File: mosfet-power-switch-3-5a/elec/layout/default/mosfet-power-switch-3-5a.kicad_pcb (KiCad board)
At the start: 2 copper layers, 225.7 x 100.8 mm, 0 parts

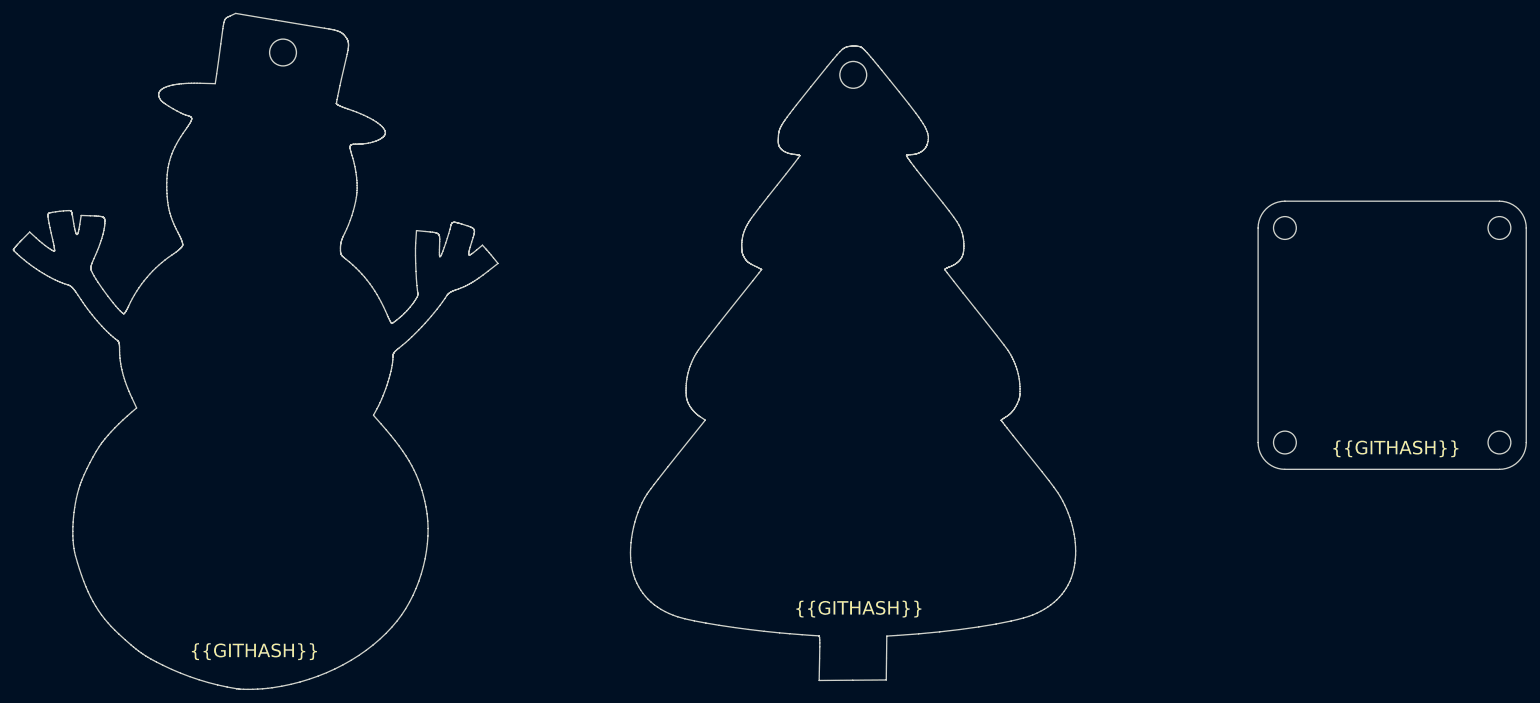
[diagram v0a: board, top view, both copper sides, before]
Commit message: placed components on board
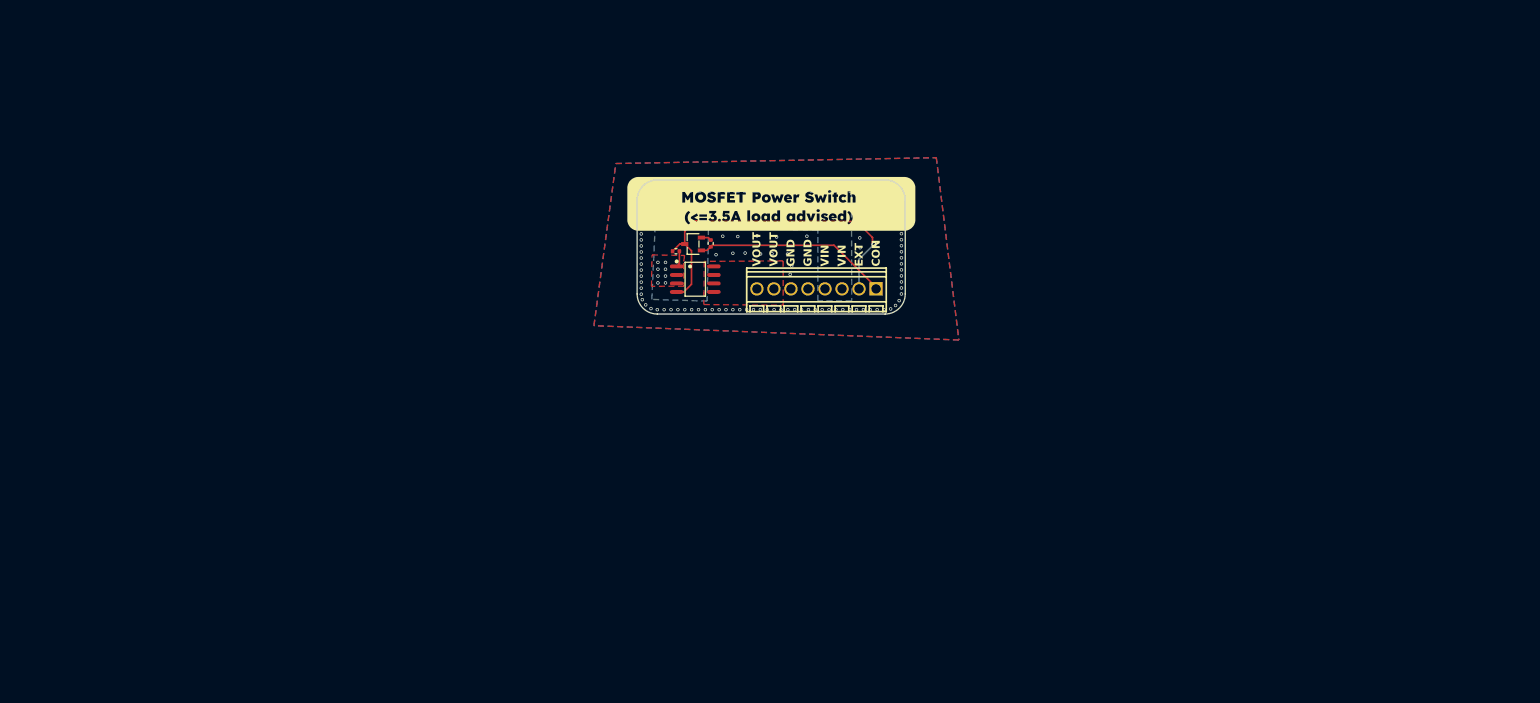
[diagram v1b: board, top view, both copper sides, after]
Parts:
- added Q1: , lib:SOIC-8_L4.9-W3.9-P1.27-LS6.0-BL, F.Cu at (137.7, 89.4)
- added Q2: , lib:SOT-23-3_L2.9-W1.6-P1.90-LS2.8-BR, F.Cu at (137.3, 84.2)
- added R1: 62.5mW Thick Film Resistors 50V ±100ppm/℃ ±1% 100kΩ 0402 Ch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, lib:R0402, F.Cu at (134.8, 85.3)
- added R2: 62.5mW Thick Film Resistors 50V ±100ppm/℃ ±1% 100kΩ 0402 Ch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, lib:R0402, F.Cu at (140.0, 84.1)
- added U1: , lib:CONN-TH_XY308-2.54-8P, F.Cu at (155.7, 90.9)
- added U2: , lib:MountingHole_3.2mm_M3, F.Cu at (133.2, 78.8)
- added U3: , lib:MountingHole_3.2mm_M3, F.Cu at (164.7, 78.9)
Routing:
- net _2: track 0.00 -> 51.8 mm, vias 0 -> 1
- net control: track 0.00 -> 29.3 mm
- net mosfet_power_switch-vcc: track 0.00 -> 2.43 mm, vias 0 -> 8
- net gnd: track 0.00 -> 1.53 mm, vias 0 -> 159
- added copper zone on B.Cu, net gnd
- added copper zone on F.Cu, net gnd
- added copper zone on B.Cu, net mosfet_power_switch-vcc
- added copper zone on F.Cu, net mosfet_power_switch-vcc
- added copper zone on F.Cu, net mosfet_power_switch-vcc-1
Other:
- board size 225.7 x 100.8 mm -> 40 x 20 mm
- board text added: "CON"
- board text added: "EXT"
- board text added: "GND"
- board text added: "Source files:"
- board text added: "VIN"
- board text added: "VOUT"
- board text added: "bit.ly/4b9zOe4"
- board text added: "designed by glowingkitty"
